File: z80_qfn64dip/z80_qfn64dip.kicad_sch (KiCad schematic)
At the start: 57 parts, among them J1 Conn_08, U1 Caravel_QFN, U2 Z80CPU, U3 TPS7A2018PDQNRM3, U4 TPS7A2033PDQNRM3, U5 TPS7A2050PDQNRM3, U6 AT25EU0081A, X1 10MHz

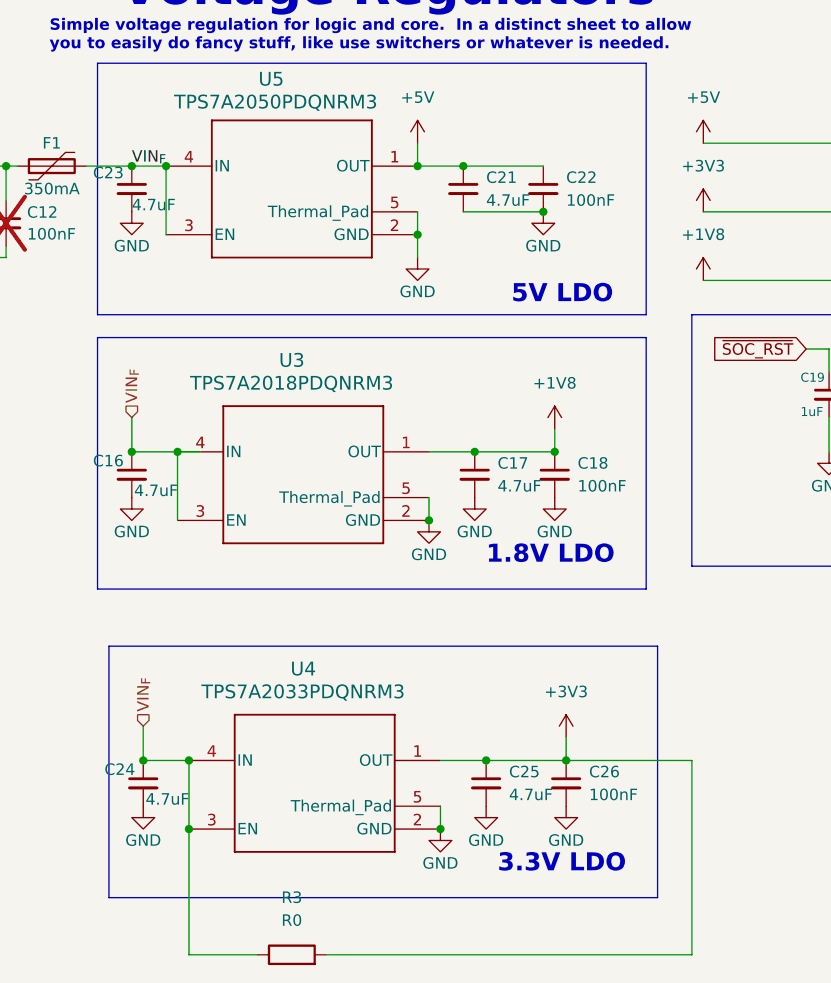
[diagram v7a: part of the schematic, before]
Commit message: add zero-ohm resistor for VDDIO as well, fill B with ground, minor changes
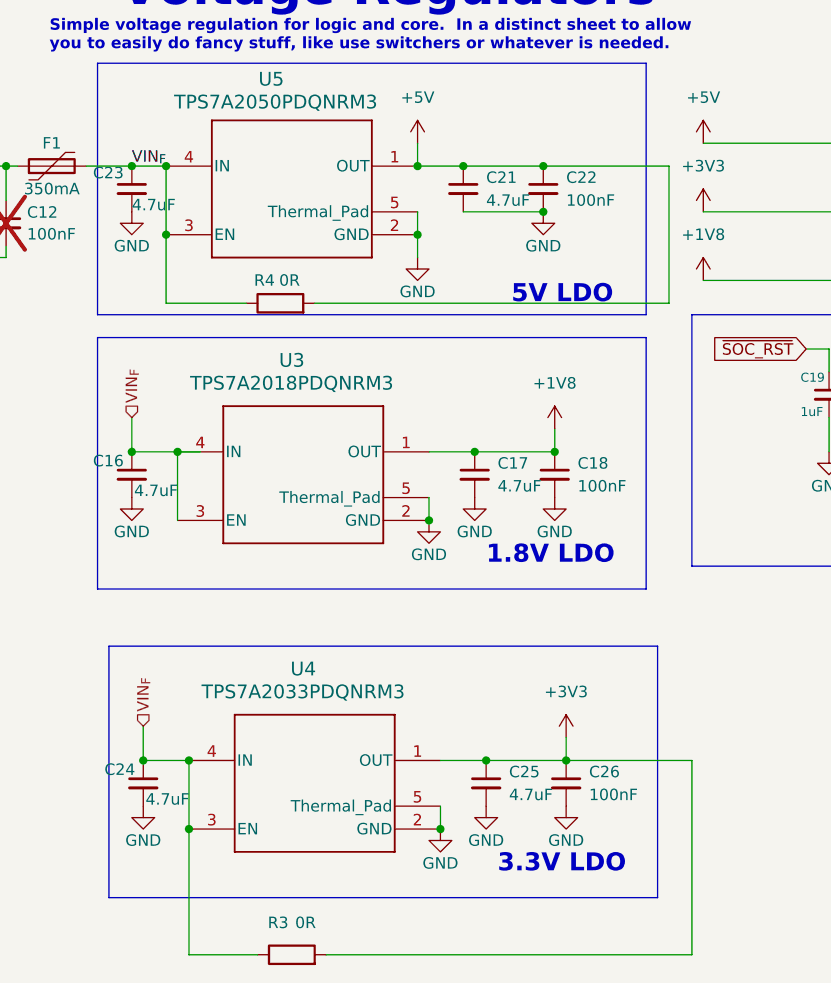
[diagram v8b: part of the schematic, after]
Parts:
- added R4: 0R, Resistor_SMD:R_0402_1005Metric_Pad0.72x0.64mm_HandSolder, symbol Device:R
- R3: value R0 -> 0R; footprint Resistor_SMD:R_0603_1608Metric_Pad0.98x0.95mm_HandSolder -> Resistor_SMD:R_0402_1005Metric_Pad0.72x0.64mm_HandSolder
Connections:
- net +5V: now also R4.2
- net VIN_{F}: now also R4.1
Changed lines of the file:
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@@
 	)
 	(junction
+		(at 87.63 148.59)
+		(diameter 0)
+		(color 0 0 0 0)
+	)
+	(junction
 		(at 78.74 148.59)
 		(diameter 0)
@@
 		(color 0 0 0 0)
 	)
+	(junction
+		(at 45.72 156.21)
+		(diameter 0)
+		(color 0 0 0 0)
+	)
 	(no_connect
 		(at 27.94 31.75)
@@
 	(wire
 		(pts
+			(xy 45.72 163.83) (xy 54.61 163.83)
+		)
+		(stroke
+			(width 0)
+			(type default)
+		)
+	)
+	(wire
+		(pts
 			(xy 80.01 27.94) (xy 86.36 27.94)
 		)
@@
 		)
 	)
+	(wire
+		(pts
+			(xy 87.63 148.59) (xy 101.6 148.59)
+		)
+		(stroke
+			(width 0)
+			(type default)
+		)
+	)
 	(bus
 		(pts
@@
 	(wire
 		(pts
+			(xy 101.6 163.83) (xy 101.6 148.59)
+		)
+		(stroke
+			(width 0)
+			(type default)
+		)
+	)
+	(wire
+		(pts
 			(xy 22.86 148.59) (xy 22.86 152.4)
 		)
@@
 		)
 	)
+	(wire
+		(pts
+			(xy 45.72 156.21) (xy 45.72 163.83)
+		)
+		(stroke
+			(width 0)
+			(type default)
+		)
+	)
 	(bus
 		(pts
@@
 		)
 	)
+	(wire
+		(pts
+			(xy 62.23 163.83) (xy 101.6 163.83)
+		)
+		(stroke
+			(width 0)
+			(type default)
+		)
+	)
 	(bus
 		(pts
@@
 			"AAAAAAAAAAAAAAAAAAAAAAAAAAAAAAAAAAAAAAAAAAAAAAAAAAAAAAAAAAAAAAAAAAAAAAAAAAAA"
 			"AAAAAAAAAAAAAAAAAAAAAAAAAAAAAAAAAAAAAAAAAAAAAAAAAAAAAAAAAAAAAAAAAAAAAAAAAAAA"
+			"AAAAAAAAAAAAAAAAAAAAAAAAAAAAAAAAAAAAAAAAAAAAAAAAAAAAAAAAAAAAAAAAAAAAAAAAAAAA"
+			"AAAAAAAAAAAAAAAAAAAAAAAAAAAAAAAAAAAAAAAAAAAAAAAAAAAAAAAAAAAAAAAAAAAAAAAAAAAA"
+			"AAAAAAAAAAAAAAAAAAAAAAAAAAAAAAAAAAAAAAAAAAAAAAAAAAAAAAAAAAAAAAAAAAAAAAAAAAAA"
+			"AAAAAAAAAAAAAAAAAAAAAAAAAAAAAAAAAAAAAAAAAAAAAAAAAAAAAAAAAAAAAAAAAAAAAAAAAAAA"
+			"AAAAAAAAAAAAAAAAAAAAAAAAAAAAAAAAAAAAAAAAAAAAAAAAAAAAAAAAAAAAAAAAAAAAAAAAAAAA"
+			"AAAAAAAAAAAAAAAAAAAAAAAAAAAAAAAAAAAAAAAAAAAAAAAAAAAAAAAAAAAAAAAAAAAAAAAAAAAA"
+			"AAAAAAAAAAAAAAAAAAAAAAAAAAAAAAAAAAAAAAAAAAAAAAAAAAAAAAAAAAAAAAAAAAAAAAAAAAAA"
+			"AAAAAAAAAAAAAAAAAAAAAAAAAAAAAAAAAAAAAAAAAAAAAAAAAAAAAAAAAAAAAAAAAAAAAAAAAAAA"
+			"AAAAAAAAAAAAAAAAAAAAAAAAAAAAAAAAAAAAAAAAAAAAAAAAAAAAAAAAAAAAAAAAAAAAAAAAAAAA"
+			"AAAAAAAAAAAAAAAAAAAAAAAAAAAAAAAAAAAAAAAAAAAAAAAAAAAAAAAAAAAAAAAAAAAAAAAAAAAA"
+			"AAAAAAAAAAAAAAAAAAAAAAAAAAAAAAAAAAAAAAAAAAAAAAAAAAAAAAAAAAAAAAAAAAAAAAAAAAAA"
+			"AAAAAAAAAAAAAAAAAAAAAAAAAAAAAAAAAAAAAAAAAAAAAAAAAAAAAAAAAAAAAAAAAAAAAAAAAAAA"
+			"AAAAAAAAAAAAAAAAAAAAAAAAAAAAAAAAAAAAAAAAAAAAAAAAAAAAAAAAAAAAAAAAAAAAAAAAAAAA"
+			"AAAAAAAAAAAAAAAAAAAAAAAAAAAAAAAAAAAAAAAAAAAAAAAAAAAAAAAAAAAAAAAAAAAAAAAAAAAA"
+			"AAAAAAAAAAAAAAAAAAAAAAAAAAAAAAAAAAAAAAAAAAAAAAAAAAAAAAAAAAAAAAAAAAAAAAAAAAAA"
+			"AAAAAAAAAAAAAAAAAAAAAAAAAAAAAAAAAAAAAAAAAAAAAAAAAAAAAAAAAAAAAAAAAAAAAAAAAAAA"
+			"AAAAAAAAAAAAAAAAAAAAAAAAAAAAAAAAAAAAAAAAAAAAAAAAAAAAAAAAAAAAAAAAAAAAAAAAAAAA"
+			"AAAAAAAAAAAAAAAAAAAAAAAAAAAAAAAAAAAAAAAAAAAAAAAAAAAAAAAAAAAAAAAAAAAAAAAAAAAA"
 			"AAAAAAAAAAAAAAAAAAAAAAAAAAAAAAAAAAAAAAAAAA=="
 		)
@@
 	)
 	(symbol
+		(lib_id "Device:R")
+		(at 58.42 163.83 90)
+		(unit 1)
+		(exclude_from_sim no)
+		(in_bom yes)
+		(on_board yes)
+		(dnp no)
+		(property "Reference" "R4"
+			(at 56.642 161.29 90)
+			(effects
+				(font
+					(size 1.27 1.27)
+				)
+			)
+		)
+		(property "Value" "0R"
+			(at 59.436 161.29 90)
+			(effects
+				(font
+					(size 1.27 1.27)
+				)
+			)
+		)
+		(property "Footprint" "Resistor_SMD:R_0402_1005Metric_Pad0.72x0.64mm_HandSolder"
+			(at 58.42 165.608 90)
+			(effects
+				(font
+					(size 1.27 1.27)
+				)
+				(hide yes)
+			)
+		)
+		(property "Datasheet" "~"
+			(at 58.42 163.83 0)
+			(effects
+				(font
+					(size 1.27 1.27)
+				)
+				(hide yes)
+			)
+		)
+		(property "Description" "Resistor"
+			(at 58.42 163.83 0)
+			(effects
+				(font
+					(size 1.27 1.27)
+				)
+				(hide yes)
+			)
+		)
+		(pin "2"
+		)
+		(pin "1"
+		)
+		(instances
+			(project "z80_qfn64dip"
+				(path "/e5031d68-0e90-4495-a422-07a5d18aeb00"
+					(reference "R4")
+					(unit 1)
+				)
+			)
+		)
+	)
+	(symbol
 		(lib_id "tps7a2018:TPS7A2018PDQNRM3")
 		(at 46.99 180.34 0)
@@
 		(on_board yes)
 		(dnp no)
-		(fields_autoplaced yes)
 		(property "Reference" "R3"
-			(at 59.69 229.87 90)
+			(at 58.166 232.664 90)
 			(effects
 				(font
@@
 			)
 		)
-		(property "Value" "R0"
-			(at 59.69 232.41 90)
+		(property "Value" "0R"
+			(at 61.214 232.664 90)
 			(effects
 				(font
@@
 			)
 		)
-		(property "Footprint" "Resistor_SMD:R_0603_1608Metric_Pad0.98x0.95mm_HandSolder"
+		(property "Footprint" "Resistor_SMD:R_0402_1005Metric_Pad0.72x0.64mm_HandSolder"
 			(at 59.69 237.998 90)
 			(effects
